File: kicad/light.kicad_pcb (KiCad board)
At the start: 4 copper layers, 216 parts, among them J1 USB_C, J2 SM03B-SRSS-TB, J3 Barrell Jack, J4 01x04, J5 Conn_01x09_MountingPin, J6 01x04, J9 Conn_01x09_MountingPin, Q1 NMOS, Q2 NMOS, Q3 NMOS, SW1 Boot, SW2 Reset, SW3 On/Off, SW4 Mode, SW5 RotaryEncoder_Switch_MP, U1 RP2350A-QFN60, U2 TPS5405DR, U3 W25Q128JVS, U4 LBEE5KL1YN-814, U5 TPS2115ADRBR, U6 TPS2115ADRBR, U7 HDC1080, U8 MAX6818EAP_T, U9 PIR223D-S0, Y1 ABM8-272-T3

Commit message: general layout
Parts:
- removed JP10: VBUS, Jumper:SolderJumper-2_P1.3mm_Bridged_RoundedPad1.0x1.5mm
- removed JP11: VREG5, Jumper:SolderJumper-2_P1.3mm_Bridged_RoundedPad1.0x1.5mm
- removed JP6: 12v in, Jumper:SolderJumper-2_P1.3mm_Bridged_RoundedPad1.0x1.5mm
- removed JP7: 5v in, Jumper:SolderJumper-2_P1.3mm_Bridged_RoundedPad1.0x1.5mm
- JP12, JP13, JP14, JP2, JP3, JP4, JP5, TP2, TP3, TP4, TP5, TP6, TP7, TP8, TP9: moved to B.Cu
- moved TP9 62.2 mm to (122.7, 34.6)
- moved TP5 59.5 mm to (122.7, 38.2)
- moved R27 56.8 mm to (123.9, 37.8), turned to -90 degrees
- moved R28 56.4 mm to (123.9, 42.0), turned to -90 degrees
- moved TP6 55.7 mm to (122.7, 41.8)
- moved TP7 55.6 mm to (122.7, 45.3)
- moved TP2 53.3 mm to (68.5, 56.1)
- moved TP3 52.9 mm to (68.5, 58.4)
- moved JP2 52.8 mm to (81.0, 58.0), turned to -90 degrees
- moved R29 52.6 mm to (127.4, 46.2), turned to -90 degrees
- moved R30 51.9 mm to (125.0, 37.8), turned to 90 degrees
- moved R25 51.7 mm to (80.8, 54.2), turned to 180 degrees
- moved J1 51.5 mm to (59.4, 58.0), turned to -90 degrees
- moved JP13 51.4 mm to (88.5, 53.6), turned to 180 degrees
- moved R31 51.4 mm to (125.0, 42.0), turned to 90 degrees
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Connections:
- J4 pad 1: /V_RGB -> Net-(J4-Pin_4)
- J4 pad 2: Net-(J4-Pin_2) -> Net-(J4-Pin_3)
- J4 pad 3: Net-(J4-Pin_3) -> Net-(J4-Pin_2)
- J4 pad 4: Net-(J4-Pin_4) -> /V_RGB
- JP2 pad 1: +3V3 -> Net-(JP2-A)
- R23 pad 1: Net-(U5-STAT) -> Net-(JP2-A)
- U5 pad 1: Net-(U5-STAT) -> Net-(JP2-A)
- U5 pad 6: Net-(JP11-B) -> /VREG5
- U5 pad 8: Net-(JP10-B) -> /VBUS
- U6 pad 6: Net-(JP7-B) -> /VREG5
- U6 pad 8: Net-(JP6-B) -> +12V

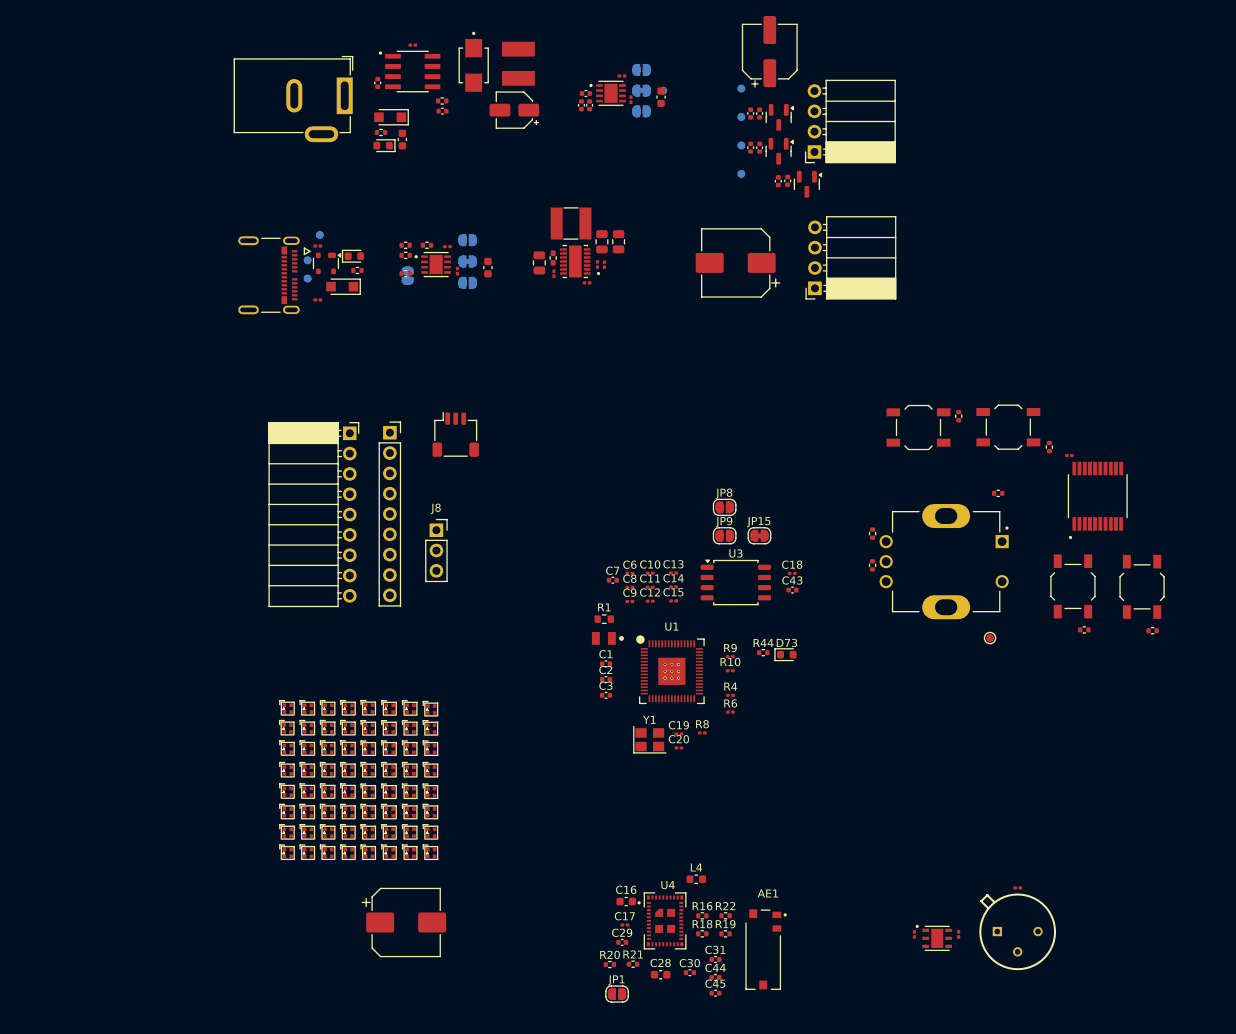
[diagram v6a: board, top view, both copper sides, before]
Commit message: change rgb to 2x4 pins; general layout
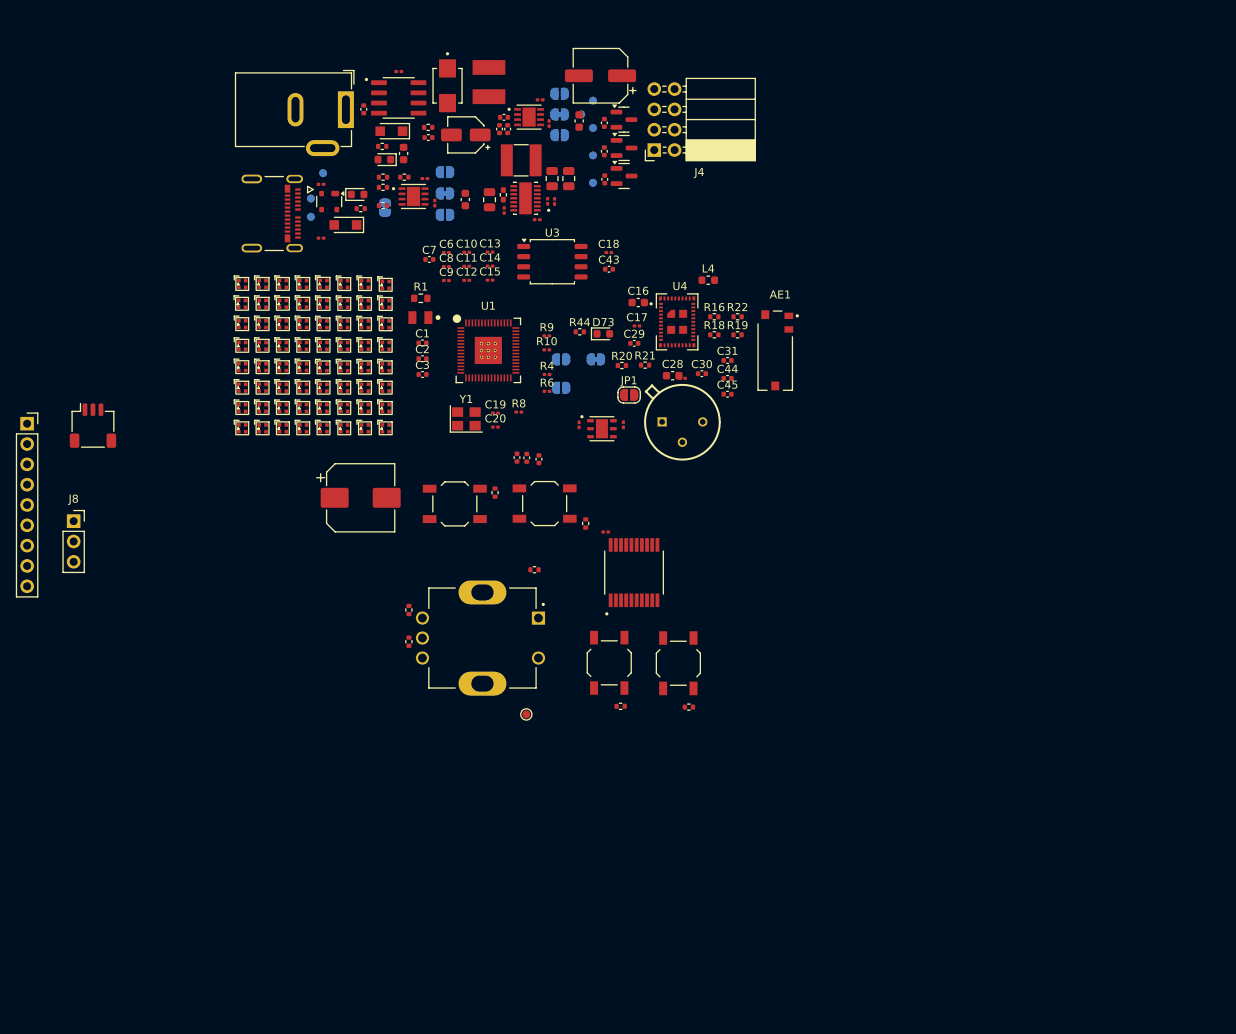
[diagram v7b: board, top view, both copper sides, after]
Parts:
- removed C40: 1000u, Capacitor_SMD:CP_Elec_8x10
- removed J5: Conn_01x09_MountingPin, Connector_PinSocket_2.54mm:PinSocket_1x09_P2.54mm_Horizontal
- removed J6: 01x04, Connector_PinSocket_2.54mm:PinSocket_1x04_P2.54mm_Horizontal
- J4: footprint Connector_PinSocket_2.54mm:PinSocket_1x04_P2.54mm_Horizontal -> Connector_PinSocket_2.54mm:PinSocket_2x04_P2.54mm_Horizontal
- JP15, JP8, JP9: moved to B.Cu
- moved C41 76.3 mm to (115.4, 70.9)
- moved U7 76.3 mm to (105.3, 77.2)
- moved R36 76.3 mm to (102.5, 76.7)
- moved R37 76.3 mm to (108.0, 76.7)
- moved U9 76.3 mm to (115.4, 77.6)
- moved C17 74.9 mm to (109.7, 64.3)
- moved C29 74.9 mm to (109.3, 66.5)
- moved C44 74.9 mm to (121.0, 70.9)
- moved C45 74.9 mm to (121.0, 72.8)
- moved R20 74.9 mm to (107.8, 69.3)
- moved AE1 74.9 mm to (127.0, 67.4)
- moved C28 74.9 mm to (114.2, 70.5)
- moved C30 74.9 mm to (117.8, 70.3)
- moved C31 74.9 mm to (121.0, 68.6)
- moved JP1 74.9 mm to (108.7, 72.9)
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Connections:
- J4 pad 2: Net-(J4-Pin_3) -> GND
- J4 pad 3: Net-(J4-Pin_2) -> Net-(J4-Pin_5)
- J4 pad 4: /V_RGB -> unconnected-(J4-Pin_6-Pad4)
- Q1 pad 1: Net-(J4-Pin_2) -> Net-(J4-Pin_3)
- Q2 pad 1: Net-(J4-Pin_3) -> Net-(J4-Pin_5)

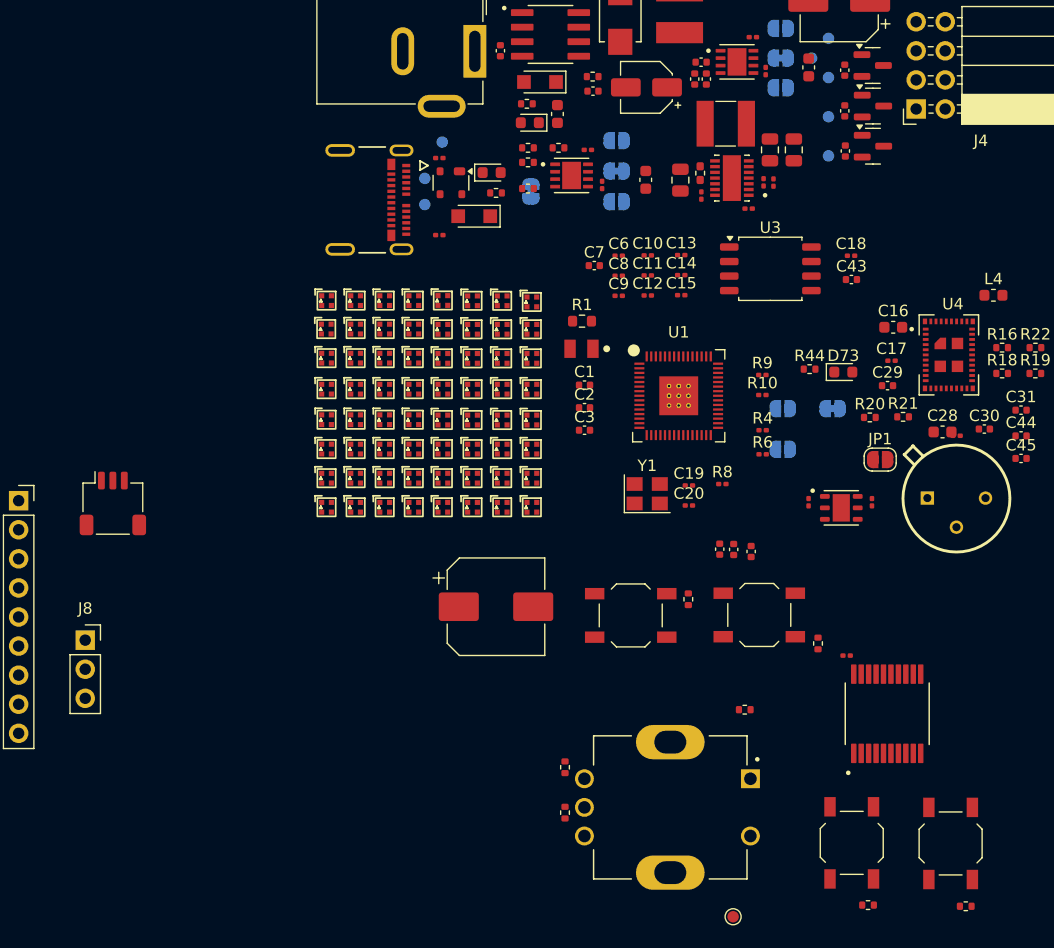
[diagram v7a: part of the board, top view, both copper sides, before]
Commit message: organize RP2350 group layout
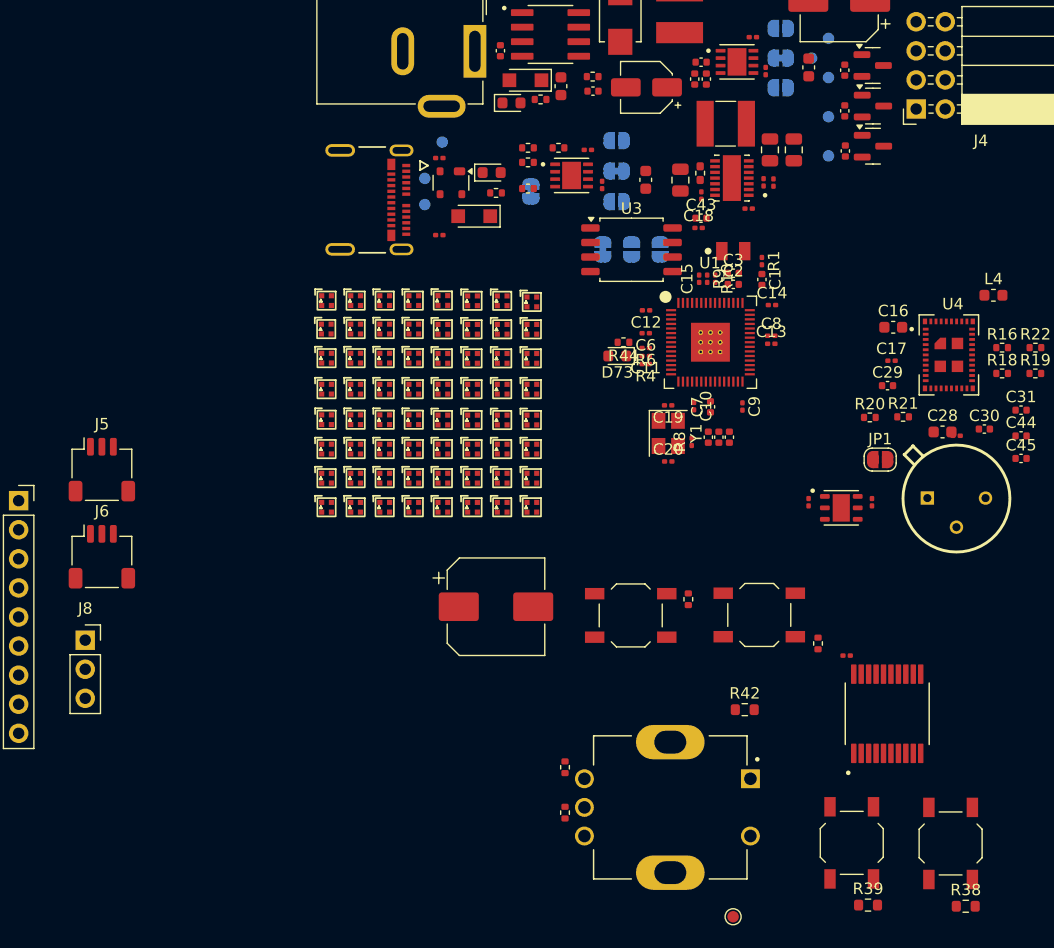
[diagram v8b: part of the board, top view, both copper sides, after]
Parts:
- removed J2: SM03B-SRSS-TB, Connector_JST:JST_SH_SM03B-SRSS-TB_1x03-1MP_P1.00mm_Horizontal
- added J5: SM03B-SRSS-TB, Connector_JST:JST_SH_SM03B-SRSS-TB_1x03-1MP_P1.00mm_Horizontal, F.Cu at (40.7, 73.8)
- added J6: SM03B-SRSS-TB, Connector_JST:JST_SH_SM03B-SRSS-TB_1x03-1MP_P1.00mm_Horizontal, F.Cu at (40.7, 81.4)
- R1: footprint Resistor_SMD:R_0603_1608Metric -> Resistor_SMD:R_0201_0603Metric
- R38, R39, R42: footprint Resistor_SMD:R_0402_1005Metric -> Resistor_SMD:R_0603_1608Metric
- moved JP15 24.4 mm to (84.5, 54.6), turned to 90 degrees
- moved JP8 20.5 mm to (89.5, 54.6), turned to -90 degrees
- moved D73 19.8 mm to (85.7, 63.9), turned to 180 degrees
- moved JP9 19.2 mm to (87.0, 54.6), turned to -90 degrees
- moved C3 18.9 mm to (95.9, 56.7)
- moved C1 18.0 mm to (98.4, 57.2), turned to -90 degrees
- moved C2 16.9 mm to (95.9, 57.6)
- moved R1 16.6 mm to (98.4, 55.6), turned to -90 degrees
- moved R44 16.4 mm to (86.3, 62.7), turned to 180 degrees
- moved C7 16.0 mm to (93.9, 68.3), turned to 90 degrees
- moved L1 15.8 mm to (95.9, 54.7), turned to 180 degrees
- moved C9 14.5 mm to (96.7, 68.3), turned to -90 degrees
- moved C8 14.3 mm to (99.2, 62.1)
- moved C43 14.2 mm to (93.1, 51.9)
- moved R6 13.8 mm to (88.2, 63.2), turned to 180 degrees
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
